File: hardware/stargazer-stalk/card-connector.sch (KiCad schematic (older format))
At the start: 7 parts, among them J5 swd-basic, U17 SN74LVC125AD, U18 pmod-interface-type-2a

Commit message: Working before reworking to a 4 card system
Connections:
- net CIPOx: now also U17.5 (2A); no longer U17.2 (1A)
- net COPIx: now also U17.8 (3Y); no longer U17.6 (2Y)
- net SCKx: now also U17.3 (1Y); no longer U17.8 (3Y)
- net CIPO1 renamed CIPO
- net CIPO: now also U17.6 (2Y); no longer U17.3 (1Y)
- net COPI1 renamed COPI
- net COPI: now also U17.9 (3A); no longer U17.5 (2A)
- net CSn1 renamed CSn
- net GO1 renamed GO
- net RST1 renamed RST
- net SCK1 renamed SCK
- net SCK: now also U17.2 (1A); no longer U17.9 (3A)
- net SWCLK1 renamed SWCLK
- net SWDIO1 renamed SWDIO
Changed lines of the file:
@@
 $Descr A4 11693 8268
 encoding utf-8
-Sheet 5 9
+Sheet 8 9
 Title ""
 Date ""
@@
 AR Path="/5F881137/5FC8FF86" Ref="U12"  Part="1"
 AR Path="/5F881143/5FC8FF86" Ref="U14"  Part="1"
-F 0 "U6" H 3200 2965 50  0000 C CNN
+F 0 "U12" H 3200 2965 50  0000 C CNN
 F 1 "pmod-interface-type-2a" H 3200 2850 50  0001 C CNN
 F 2 "stargazer-stalk:pmod-double" H 3200 2850 50  0001 C CNN
@@
 AR Path="/5F881137/5FC8FF8C" Ref="#PWR0178"  Part="1"
 AR Path="/5F881143/5FC8FF8C" Ref="#PWR0192"  Part="1"
-F 0 "#PWR0136" H 4000 2550 50  0001 C CNN
+F 0 "#PWR0178" H 4000 2550 50  0001 C CNN
 F 1 "+5V" H 4015 2873 50  0000 C CNN
 F 2 "" H 4000 2700 50  0001 C CNN
@@
 AR Path="/5F881137/5FC8FF96" Ref="#PWR0179"  Part="1"
 AR Path="/5F881143/5FC8FF96" Ref="#PWR0193"  Part="1"
-F 0 "#PWR0137" H 2550 2550 50  0001 C CNN
+F 0 "#PWR0179" H 2550 2550 50  0001 C CNN
 F 1 "GND" H 2555 2627 50  0000 C CNN
 F 2 "" H 2550 2800 50  0001 C CNN
@@
 AR Path="/5F881137/5FC8FF9C" Ref="#PWR0180"  Part="1"
 AR Path="/5F881143/5FC8FF9C" Ref="#PWR0194"  Part="1"
-F 0 "#PWR0138" H 2450 2550 50  0001 C CNN
+F 0 "#PWR0180" H 2450 2550 50  0001 C CNN
 F 1 "+5V" H 2465 2873 50  0000 C CNN
 F 2 "" H 2450 2700 50  0001 C CNN
@@
 $EndComp
 Text Label 3600 2500 0    50   ~ 0
-SWCLK1
+SWCLK
 Text Label 3600 2400 0    50   ~ 0
-SWDIO1
+SWDIO
 Text Label 3600 2300 0    50   ~ 0
-RST1
+RST
 Text Label 3600 2200 0    50   ~ 0
-GO1
+GO
 Text Label 2800 2400 2    50   ~ 0
-CIPO1
+CIPO
 Text Label 2800 2500 2    50   ~ 0
-SCK1
+SCK
 $Comp
 L stargazer:SN74LVC125AD U17
@@
 AR Path="/5F881137/5FC8FFAA" Ref="U11"  Part="1"
 AR Path="/5F881143/5FC8FFAA" Ref="U13"  Part="1"
-F 0 "U5" H 2450 4315 50  0000 C CNN
+F 0 "U11" H 2450 4315 50  0000 C CNN
 F 1 "SN74LVC125AD" H 2450 4224 50  0000 C CNN
 F 2 "Package_SO:SOIC-14_3.9x8.7mm_P1.27mm" H 2450 4223 50  0001 C CNN
@@
 $EndComp
 Text Label 2050 4150 2    50   ~ 0
-GO1
+GO
 Text Label 2050 4450 2    50   ~ 0
-GO1
+GO
 Text Label 2850 4250 0    50   ~ 0
-GO1
+GO
 Text Label 2850 4550 0    50   ~ 0
-GO1
+GO
+Text Label 2050 4650 2    50   ~ 0
+CIPO
+Text Label 2850 4650 0    50   ~ 0
+COPI
+Text Label 2050 4250 2    50   ~ 0
+SCK
+Text Label 2850 4350 0    50   ~ 0
+CSn
+Text Label 2050 4550 2    50   ~ 0
+CIPOx
+Text Label 2850 4750 0    50   ~ 0
+COPIx
 Text Label 2050 4350 2    50   ~ 0
-CIPO1
-Text Label 2050 4550 2    50   ~ 0
-COPI1
-Text Label 2850 4650 0    50   ~ 0
-SCK1
-Text Label 2850 4350 0    50   ~ 0
-CSn1
-Text Label 2050 4250 2    50   ~ 0
-CIPOx
-Text Label 2050 4650 2    50   ~ 0
-COPIx
-Text Label 2850 4750 0    50   ~ 0
 SCKx
 Text Label 2850 4450 0    50   ~ 0
@@
 AR Path="/5F881137/5FC8FFBC" Ref="#PWR0181"  Part="1"
 AR Path="/5F881143/5FC8FFBC" Ref="#PWR0195"  Part="1"
-F 0 "#PWR0139" H 2050 4650 50  0001 C CNN
+F 0 "#PWR0181" H 2050 4650 50  0001 C CNN
 F 1 "GND" H 2055 4727 50  0000 C CNN
 F 2 "" H 2050 4900 50  0001 C CNN
@@
 AR Path="/5F881137/5FC8FFC3" Ref="#PWR0182"  Part="1"
 AR Path="/5F881143/5FC8FFC3" Ref="#PWR0196"  Part="1"
-F 0 "#PWR0140" H 2850 3750 50  0001 C CNN
+F 0 "#PWR0182" H 2850 3750 50  0001 C CNN
 F 1 "+3V3" H 2865 4073 50  0000 C CNN
 F 2 "" H 2850 3900 50  0001 C CNN
@@
 AR Path="/5F881137/5FC8FFCA" Ref="#PWR0183"  Part="1"
 AR Path="/5F881143/5FC8FFCA" Ref="#PWR0197"  Part="1"
-F 0 "#PWR0141" H 3900 2550 50  0001 C CNN
+F 0 "#PWR0183" H 3900 2550 50  0001 C CNN
 F 1 "GND" H 3905 2627 50  0000 C CNN
 F 2 "" H 3900 2800 50  0001 C CNN
@@
 AR Path="/5F881137/5FC98BCD" Ref="#PWR0184"  Part="1"
 AR Path="/5F881143/5FC98BCD" Ref="#PWR0198"  Part="1"
-F 0 "#PWR0142" H 5300 1500 50  0001 C CNN
+F 0 "#PWR0184" H 5300 1500 50  0001 C CNN
 F 1 "+3V3" H 5315 1823 50  0000 C CNN
 F 2 "" H 5300 1650 50  0001 C CNN
@@
 AR Path="/5F881137/5FC98BD3" Ref="R26"  Part="1"
 AR Path="/5F881143/5FC98BD3" Ref="R29"  Part="1"
-F 0 "R13" V 5093 2000 50  0000 C CNN
+F 0 "R26" V 5093 2000 50  0000 C CNN
 F 1 "100k" V 5184 2000 50  0000 C CNN
 F 2 "Resistor_SMD:R_0805_2012Metric" V 5230 2000 50  0001 C CNN
@@
 AR Path="/5F881137/5FC98BD9" Ref="R25"  Part="1"
 AR Path="/5F881143/5FC98BD9" Ref="R28"  Part="1"
-F 0 "R8" V 4543 2000 50  0000 C CNN
+F 0 "R25" V 4543 2000 50  0000 C CNN
 F 1 "100k" V 4634 2000 50  0000 C CNN
 F 2 "Resistor_SMD:R_0805_2012Metric" V 4680 2000 50  0001 C CNN
@@
 AR Path="/5F881137/5FC98BDF" Ref="R20"  Part="1"
 AR Path="/5F881143/5FC98BDF" Ref="R27"  Part="1"
-F 0 "R7" V 4243 2000 50  0000 C CNN
+F 0 "R20" V 4243 2000 50  0000 C CNN
 F 1 "100k" V 4334 2000 50  0000 C CNN
 F 2 "Resistor_SMD:R_0805_2012Metric" V 4380 2000 50  0001 C CNN
@@
 $EndComp
 Text Label 4450 1850 1    50   ~ 0
-COPI1
+COPI
 Text Label 4750 1850 1    50   ~ 0
-SCK1
+SCK
 Text Label 5300 2150 3    50   ~ 0
-CSn1
+CSn
 $Comp
 L power:+3V3 #PWR?
@@
 AR Path="/5F881137/5FC9DA3A" Ref="#PWR0185"  Part="1"
 AR Path="/5F881143/5FC9DA3A" Ref="#PWR0199"  Part="1"
-F 0 "#PWR0143" H 4000 4150 50  0001 C CNN
+F 0 "#PWR0185" H 4000 4150 50  0001 C CNN
 F 1 "+3V3" H 4015 4473 50  0000 C CNN
 F 2 "" H 4000 4300 50  0001 C CNN
@@
 AR Path="/5F881137/5FC9DA40" Ref="#PWR0186"  Part="1"
 AR Path="/5F881143/5FC9DA40" Ref="#PWR0200"  Part="1"
-F 0 "#PWR0144" H 4000 4350 50  0001 C CNN
+F 0 "#PWR0186" H 4000 4350 50  0001 C CNN
 F 1 "GND" H 4005 4427 50  0000 C CNN
 F 2 "" H 4000 4600 50  0001 C CNN
@@
 AR Path="/5F881137/5FC9DA52" Ref="C7"  Part="1"
 AR Path="/5F881143/5FC9DA52" Ref="C8"  Part="1"
-F 0 "C4" H 4115 4496 50  0000 L CNN
+F 0 "C7" H 4115 4496 50  0000 L CNN
 F 1 "0.1uF" H 4115 4405 50  0000 L CNN
 F 2 "Capacitor_SMD:C_0805_2012Metric" H 4038 4300 50  0001 C CNN
@@
 AR Path="/5F881137/5FCA2EE2" Ref="#PWR0187"  Part="1"
 AR Path="/5F881143/5FCA2EE2" Ref="#PWR0201"  Part="1"
-F 0 "#PWR0145" H 4600 2000 50  0001 C CNN
+F 0 "#PWR0187" H 4600 2000 50  0001 C CNN
 F 1 "GND" H 4605 2077 50  0000 C CNN
 F 2 "" H 4600 2250 50  0001 C CNN
@@
 $EndComp
 Text Label 2800 2300 2    50   ~ 0
-COPI1
+COPI
 Text Label 2800 2200 2    50   ~ 0
-CSn1
+CSn
 Text Label 1150 1800 0    50   ~ 0
 CSnx
@@
 AR Path="/5F881137/5FCB57B7" Ref="#PWR0188"  Part="1"
 AR Path="/5F881143/5FCB57B7" Ref="#PWR0202"  Part="1"
-F 0 "#PWR0146" H 1500 1100 50  0001 C CNN
+F 0 "#PWR0188" H 1500 1100 50  0001 C CNN
 F 1 "+5V" H 1515 1423 50  0000 C CNN
 F 2 "" H 1500 1250 50  0001 C CNN
@@
 AR Path="/5F881137/5FCB5BD1" Ref="#PWR0189"  Part="1"
 AR Path="/5F881143/5FCB5BD1" Ref="#PWR0203"  Part="1"
-F 0 "#PWR0147" H 1650 1200 50  0001 C CNN
+F 0 "#PWR0189" H 1650 1200 50  0001 C CNN
 F 1 "+3V3" H 1665 1523 50  0000 C CNN
 F 2 "" H 1650 1350 50  0001 C CNN
@@
 AR Path="/5F881137/5FCB603A" Ref="#PWR0190"  Part="1"
 AR Path="/5F881143/5FCB603A" Ref="#PWR0204"  Part="1"
-F 0 "#PWR0148" H 1500 1200 50  0001 C CNN
+F 0 "#PWR0190" H 1500 1200 50  0001 C CNN
 F 1 "GND" H 1505 1277 50  0000 C CNN
 F 2 "" H 1500 1450 50  0001 C CNN
@@
 	950  2200 1150 2200
 Text Label 6300 4050 0    50   ~ 0
-SWCLK1
+SWCLK
 Text Label 6300 3950 0    50   ~ 0
-SWDIO1
+SWDIO
 Text Label 6300 3750 0    50   ~ 0
-RST1
+RST
 $Comp
 L stargazer-stalk:swd-basic J5
@@
 AR Path="/5F881137/5F9606F1" Ref="J7"  Part="1"
 AR Path="/5F881143/5F9606F1" Ref="J8"  Part="1"
-F 0 "J4" V 6265 3667 50  0000 C CNN
+F 0 "J7" V 6265 3667 50  0000 C CNN
 F 1 "swd-basic" V 6174 3667 50  0000 C CNN
 F 2 "Connector_PinHeader_2.54mm:PinHeader_1x04_P2.54mm_Vertical" H 5850 3950 50  0001 C CNN
@@
 AR Path="/5F881137/5F961C5A" Ref="#PWR0191"  Part="1"
 AR Path="/5F881143/5F961C5A" Ref="#PWR0205"  Part="1"
-F 0 "#PWR0149" H 6850 3600 50  0001 C CNN
+F 0 "#PWR0191" H 6850 3600 50  0001 C CNN
 F 1 "GND" H 6855 3677 50  0000 C CNN
 F 2 "" H 6850 3850 50  0001 C CNN

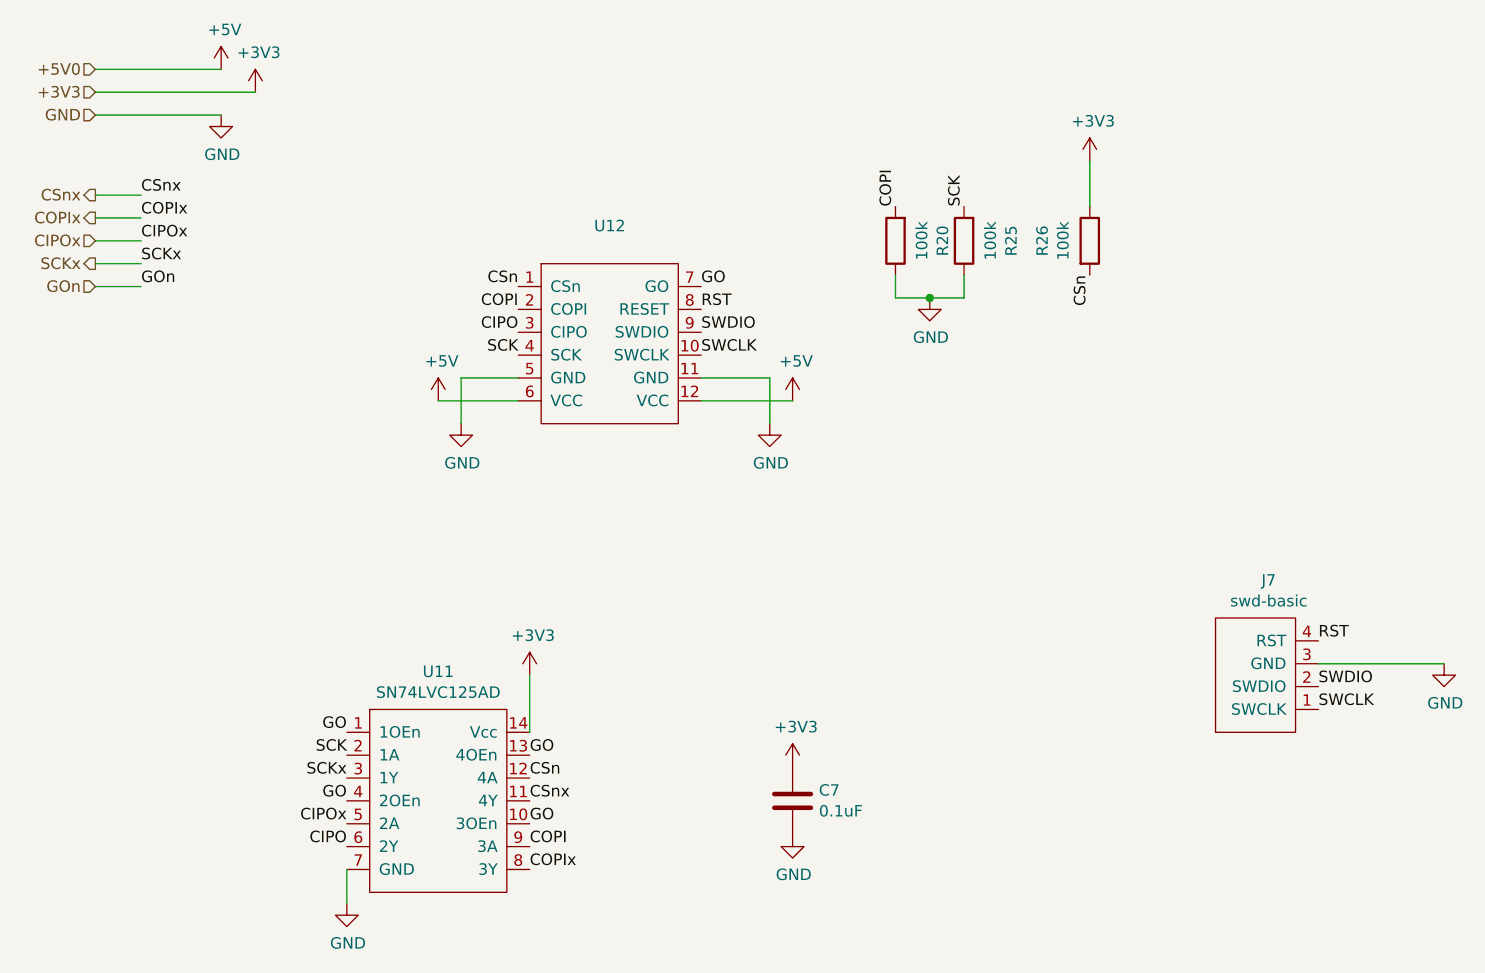
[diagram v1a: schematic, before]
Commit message: Finished routing, but it's probably too much for 2 layers
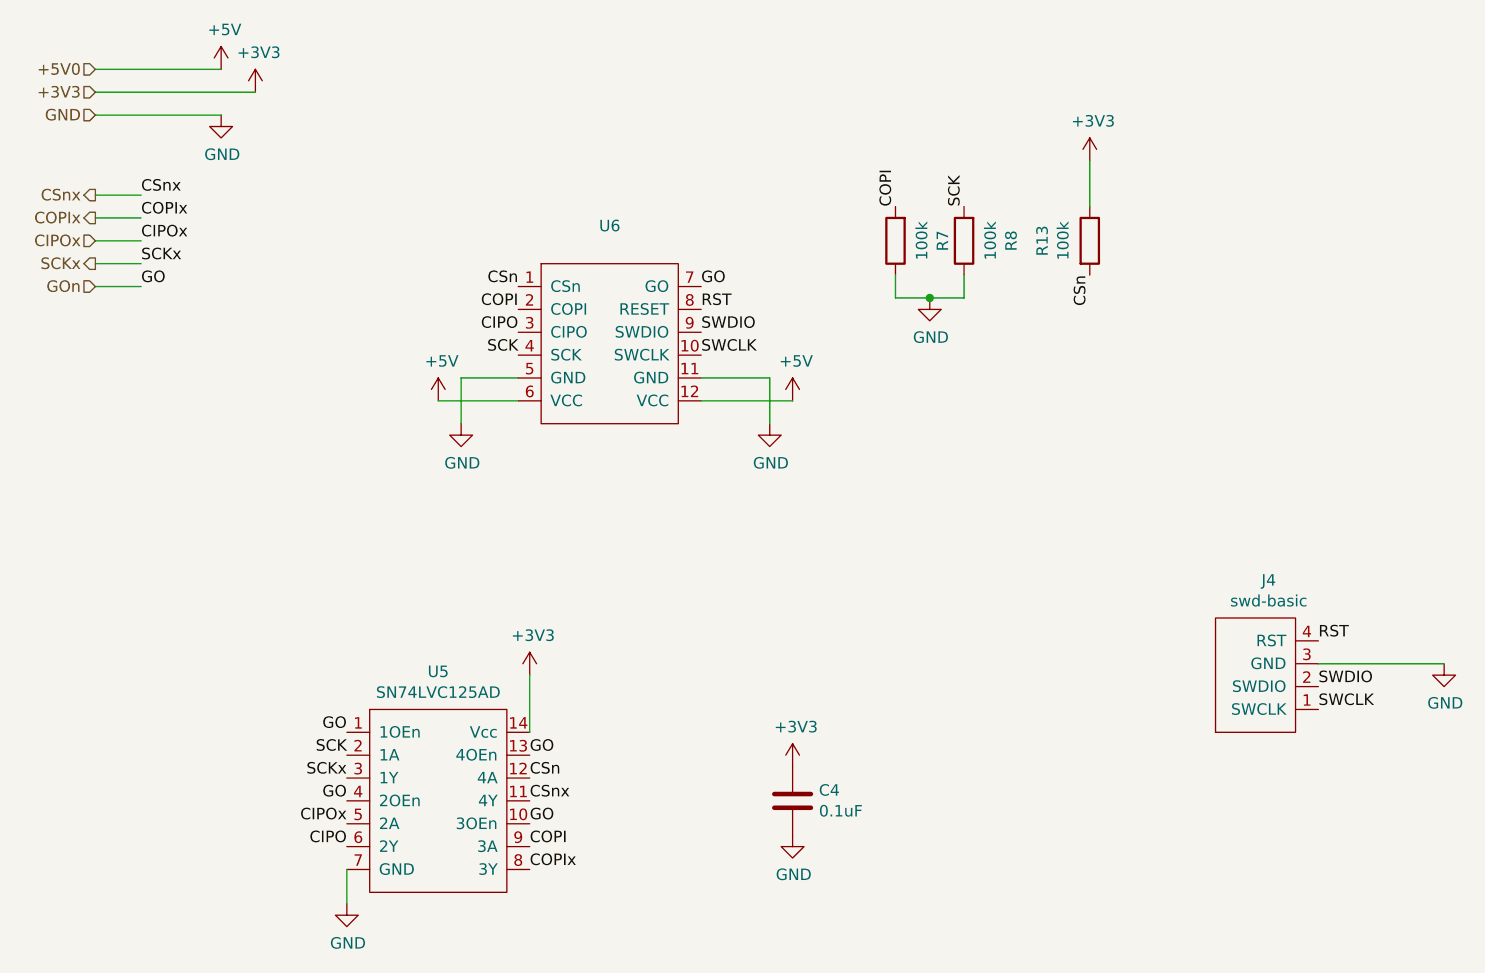
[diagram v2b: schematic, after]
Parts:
- U18: footprint stargazer-stalk:pmod-double -> stargazer-stalk:pmod-double-vertical
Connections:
- net GO is gone; now on net GOn: U17.1 (1OEn), U17.10 (3OEn), U17.13 (4OEn), U17.4 (2OEn), U18.7 (GO)
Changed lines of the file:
@@
 $Descr A4 11693 8268
 encoding utf-8
-Sheet 8 9
+Sheet 3 7
 Title ""
 Date ""
@@
 AR Path="/5F881137/5FC8FF86" Ref="U12"  Part="1"
 AR Path="/5F881143/5FC8FF86" Ref="U14"  Part="1"
-F 0 "U12" H 3200 2965 50  0000 C CNN
+F 0 "U6" H 3200 2965 50  0000 C CNN
 F 1 "pmod-interface-type-2a" H 3200 2850 50  0001 C CNN
-F 2 "stargazer-stalk:pmod-double" H 3200 2850 50  0001 C CNN
+F 2 "stargazer-stalk:pmod-double-vertical" H 3200 2850 50  0001 C CNN
 F 3 "" H 3200 2850 50  0001 C CNN
 	1    3200 2450
@@
 AR Path="/5F881137/5FC8FF8C" Ref="#PWR0178"  Part="1"
 AR Path="/5F881143/5FC8FF8C" Ref="#PWR0192"  Part="1"
-F 0 "#PWR0178" H 4000 2550 50  0001 C CNN
+F 0 "#PWR0136" H 4000 2550 50  0001 C CNN
 F 1 "+5V" H 4015 2873 50  0000 C CNN
 F 2 "" H 4000 2700 50  0001 C CNN
@@
 AR Path="/5F881137/5FC8FF96" Ref="#PWR0179"  Part="1"
 AR Path="/5F881143/5FC8FF96" Ref="#PWR0193"  Part="1"
-F 0 "#PWR0179" H 2550 2550 50  0001 C CNN
+F 0 "#PWR0137" H 2550 2550 50  0001 C CNN
 F 1 "GND" H 2555 2627 50  0000 C CNN
 F 2 "" H 2550 2800 50  0001 C CNN
@@
 AR Path="/5F881137/5FC8FF9C" Ref="#PWR0180"  Part="1"
 AR Path="/5F881143/5FC8FF9C" Ref="#PWR0194"  Part="1"
-F 0 "#PWR0180" H 2450 2550 50  0001 C CNN
+F 0 "#PWR0138" H 2450 2550 50  0001 C CNN
 F 1 "+5V" H 2465 2873 50  0000 C CNN
 F 2 "" H 2450 2700 50  0001 C CNN
@@
 AR Path="/5F881137/5FC8FFAA" Ref="U11"  Part="1"
 AR Path="/5F881143/5FC8FFAA" Ref="U13"  Part="1"
-F 0 "U11" H 2450 4315 50  0000 C CNN
+F 0 "U5" H 2450 4315 50  0000 C CNN
 F 1 "SN74LVC125AD" H 2450 4224 50  0000 C CNN
 F 2 "Package_SO:SOIC-14_3.9x8.7mm_P1.27mm" H 2450 4223 50  0001 C CNN
@@
 AR Path="/5F881137/5FC8FFBC" Ref="#PWR0181"  Part="1"
 AR Path="/5F881143/5FC8FFBC" Ref="#PWR0195"  Part="1"
-F 0 "#PWR0181" H 2050 4650 50  0001 C CNN
+F 0 "#PWR0139" H 2050 4650 50  0001 C CNN
 F 1 "GND" H 2055 4727 50  0000 C CNN
 F 2 "" H 2050 4900 50  0001 C CNN
@@
 AR Path="/5F881137/5FC8FFC3" Ref="#PWR0182"  Part="1"
 AR Path="/5F881143/5FC8FFC3" Ref="#PWR0196"  Part="1"
-F 0 "#PWR0182" H 2850 3750 50  0001 C CNN
+F 0 "#PWR0140" H 2850 3750 50  0001 C CNN
 F 1 "+3V3" H 2865 4073 50  0000 C CNN
 F 2 "" H 2850 3900 50  0001 C CNN
@@
 AR Path="/5F881137/5FC8FFCA" Ref="#PWR0183"  Part="1"
 AR Path="/5F881143/5FC8FFCA" Ref="#PWR0197"  Part="1"
-F 0 "#PWR0183" H 3900 2550 50  0001 C CNN
+F 0 "#PWR0141" H 3900 2550 50  0001 C CNN
 F 1 "GND" H 3905 2627 50  0000 C CNN
 F 2 "" H 3900 2800 50  0001 C CNN
@@
 AR Path="/5F881137/5FC98BCD" Ref="#PWR0184"  Part="1"
 AR Path="/5F881143/5FC98BCD" Ref="#PWR0198"  Part="1"
-F 0 "#PWR0184" H 5300 1500 50  0001 C CNN
+F 0 "#PWR0142" H 5300 1500 50  0001 C CNN
 F 1 "+3V3" H 5315 1823 50  0000 C CNN
 F 2 "" H 5300 1650 50  0001 C CNN
@@
 AR Path="/5F881137/5FC98BD3" Ref="R26"  Part="1"
 AR Path="/5F881143/5FC98BD3" Ref="R29"  Part="1"
-F 0 "R26" V 5093 2000 50  0000 C CNN
+F 0 "R13" V 5093 2000 50  0000 C CNN
 F 1 "100k" V 5184 2000 50  0000 C CNN
 F 2 "Resistor_SMD:R_0805_2012Metric" V 5230 2000 50  0001 C CNN
@@
 AR Path="/5F881137/5FC98BD9" Ref="R25"  Part="1"
 AR Path="/5F881143/5FC98BD9" Ref="R28"  Part="1"
-F 0 "R25" V 4543 2000 50  0000 C CNN
+F 0 "R8" V 4543 2000 50  0000 C CNN
 F 1 "100k" V 4634 2000 50  0000 C CNN
 F 2 "Resistor_SMD:R_0805_2012Metric" V 4680 2000 50  0001 C CNN
@@
 AR Path="/5F881137/5FC98BDF" Ref="R20"  Part="1"
 AR Path="/5F881143/5FC98BDF" Ref="R27"  Part="1"
-F 0 "R20" V 4243 2000 50  0000 C CNN
+F 0 "R7" V 4243 2000 50  0000 C CNN
 F 1 "100k" V 4334 2000 50  0000 C CNN
 F 2 "Resistor_SMD:R_0805_2012Metric" V 4380 2000 50  0001 C CNN
@@
 AR Path="/5F881137/5FC9DA3A" Ref="#PWR0185"  Part="1"
 AR Path="/5F881143/5FC9DA3A" Ref="#PWR0199"  Part="1"
-F 0 "#PWR0185" H 4000 4150 50  0001 C CNN
+F 0 "#PWR0143" H 4000 4150 50  0001 C CNN
 F 1 "+3V3" H 4015 4473 50  0000 C CNN
 F 2 "" H 4000 4300 50  0001 C CNN
@@
 AR Path="/5F881137/5FC9DA40" Ref="#PWR0186"  Part="1"
 AR Path="/5F881143/5FC9DA40" Ref="#PWR0200"  Part="1"
-F 0 "#PWR0186" H 4000 4350 50  0001 C CNN
+F 0 "#PWR0144" H 4000 4350 50  0001 C CNN
 F 1 "GND" H 4005 4427 50  0000 C CNN
 F 2 "" H 4000 4600 50  0001 C CNN
@@
 AR Path="/5F881137/5FC9DA52" Ref="C7"  Part="1"
 AR Path="/5F881143/5FC9DA52" Ref="C8"  Part="1"
-F 0 "C7" H 4115 4496 50  0000 L CNN
+F 0 "C4" H 4115 4496 50  0000 L CNN
 F 1 "0.1uF" H 4115 4405 50  0000 L CNN
 F 2 "Capacitor_SMD:C_0805_2012Metric" H 4038 4300 50  0001 C CNN
@@
 AR Path="/5F881137/5FCA2EE2" Ref="#PWR0187"  Part="1"
 AR Path="/5F881143/5FCA2EE2" Ref="#PWR0201"  Part="1"
-F 0 "#PWR0187" H 4600 2000 50  0001 C CNN
+F 0 "#PWR0145" H 4600 2000 50  0001 C CNN
 F 1 "GND" H 4605 2077 50  0000 C CNN
 F 2 "" H 4600 2250 50  0001 C CNN
@@
 AR Path="/5F881137/5FCB57B7" Ref="#PWR0188"  Part="1"
 AR Path="/5F881143/5FCB57B7" Ref="#PWR0202"  Part="1"
-F 0 "#PWR0188" H 1500 1100 50  0001 C CNN
+F 0 "#PWR0146" H 1500 1100 50  0001 C CNN
 F 1 "+5V" H 1515 1423 50  0000 C CNN
 F 2 "" H 1500 1250 50  0001 C CNN
@@
 AR Path="/5F881137/5FCB5BD1" Ref="#PWR0189"  Part="1"
 AR Path="/5F881143/5FCB5BD1" Ref="#PWR0203"  Part="1"
-F 0 "#PWR0189" H 1650 1200 50  0001 C CNN
+F 0 "#PWR0147" H 1650 1200 50  0001 C CNN
 F 1 "+3V3" H 1665 1523 50  0000 C CNN
 F 2 "" H 1650 1350 50  0001 C CNN
@@
 AR Path="/5F881137/5FCB603A" Ref="#PWR0190"  Part="1"
 AR Path="/5F881143/5FCB603A" Ref="#PWR0204"  Part="1"
-F 0 "#PWR0190" H 1500 1200 50  0001 C CNN
+F 0 "#PWR0148" H 1500 1200 50  0001 C CNN
 F 1 "GND" H 1505 1277 50  0000 C CNN
 F 2 "" H 1500 1450 50  0001 C CNN
@@
 GOn
 Text Label 1150 2200 0    50   ~ 0
-GOn
+GO
 Wire Wire Line
 	950  2200 1150 2200
@@
 AR Path="/5F881137/5F9606F1" Ref="J7"  Part="1"
 AR Path="/5F881143/5F9606F1" Ref="J8"  Part="1"
-F 0 "J7" V 6265 3667 50  0000 C CNN
+F 0 "J4" V 6265 3667 50  0000 C CNN
 F 1 "swd-basic" V 6174 3667 50  0000 C CNN
 F 2 "Connector_PinHeader_2.54mm:PinHeader_1x04_P2.54mm_Vertical" H 5850 3950 50  0001 C CNN
@@
 AR Path="/5F881137/5F961C5A" Ref="#PWR0191"  Part="1"
 AR Path="/5F881143/5F961C5A" Ref="#PWR0205"  Part="1"
-F 0 "#PWR0191" H 6850 3600 50  0001 C CNN
+F 0 "#PWR0149" H 6850 3600 50  0001 C CNN
 F 1 "GND" H 6855 3677 50  0000 C CNN
 F 2 "" H 6850 3850 50  0001 C CNN
